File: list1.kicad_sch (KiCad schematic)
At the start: 3 parts, among them U1 8284A, U2 8259A, U3 8088

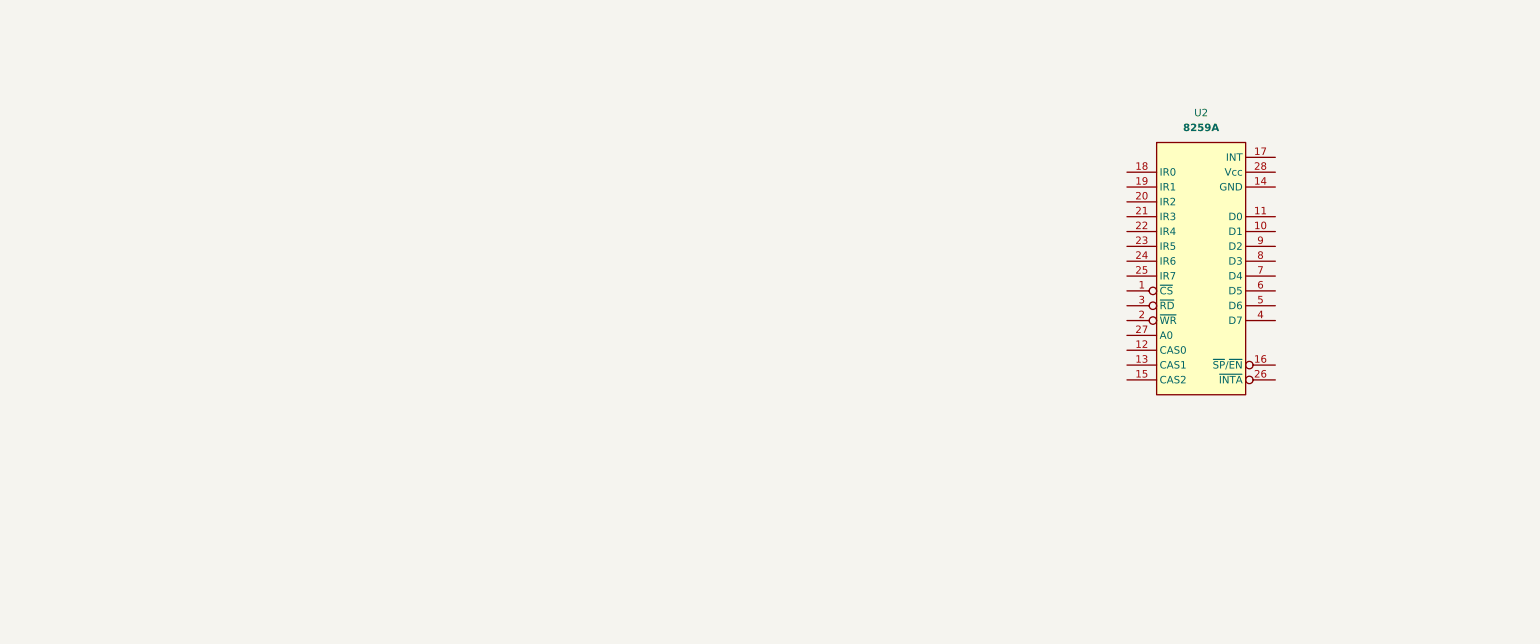
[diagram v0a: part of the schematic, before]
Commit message: Update 16.04.2024
Two datasheets added (8087 and 8288), library updated.
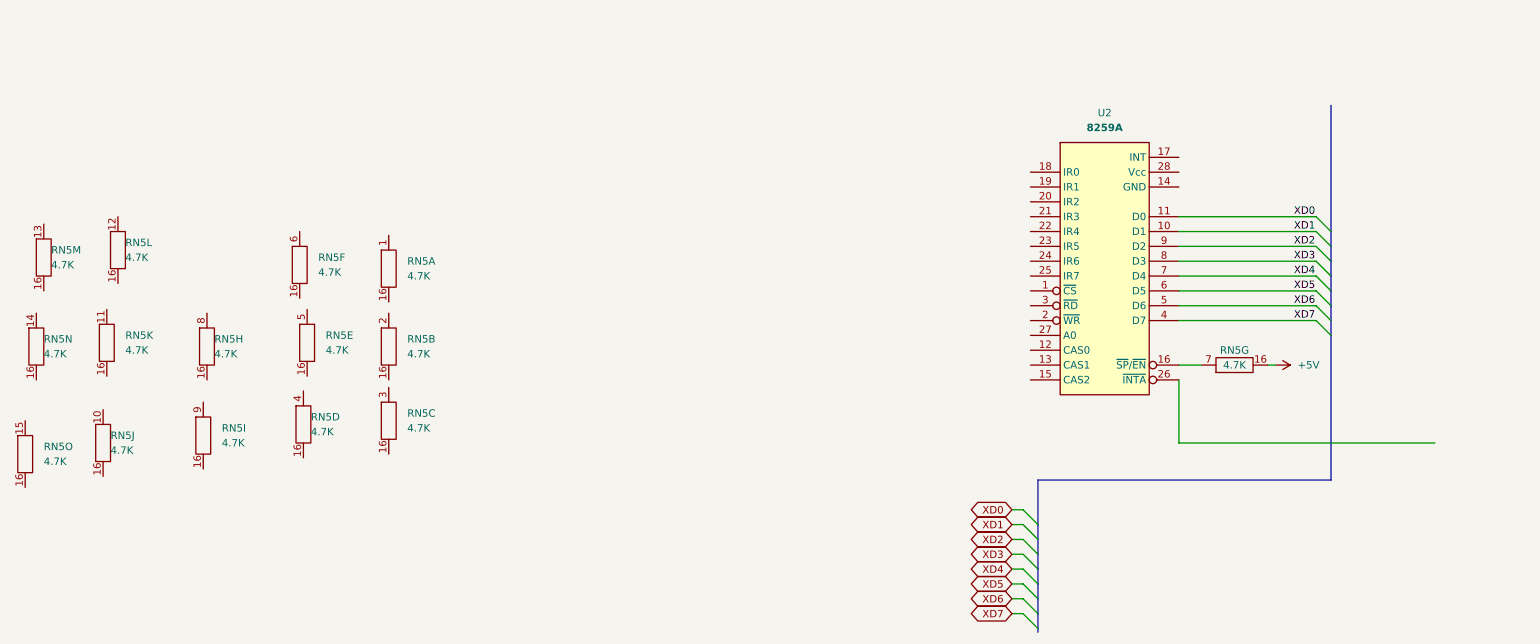
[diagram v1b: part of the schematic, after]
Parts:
- added RN5: 4.7K, Package_DIP:DIP-16_W7.62mm, symbol Mad5150_early:Resistor_Network
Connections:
- net XD1: now reaches U2.10 (D1)
- net XD0: now reaches U2.11 (D0)
- net at U2.16 (~{SP}/~{EN}): now also RN5.7
- net XD7: now reaches U2.4 (D7)
- net XD6: now reaches U2.5 (D6)
- net XD5: now reaches U2.6 (D5)
- net XD4: now reaches U2.7 (D4)
- net XD3: now reaches U2.8 (D3)
- net XD2: now reaches U2.9 (D2)
- new net +5V: RN5.16
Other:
- moved on the sheet: U2

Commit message: Update 17.04.2024
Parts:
- added C1: 5-30pf, symbol Device:C_Variable
- added R1, R2: 510, symbol Device:R
- added RN1: 4.7K, Package_DIP:DIP-16_W7.62mm, symbol Mad5150_early:Resistor_Network
- added U22: 74LS04, Package_DIP:DIP-14_W7.62mm, symbol 74xx:74LS04
- added Y1: 14.31818MHz, symbol Device:Crystal
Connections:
- net +5V: now also U1.18 (Vcc), U1.7 (~{AEN2}), U2.28 (Vcc), RN1.16
- net GND: now reaches U1.1 (CSYNC)
- net GND: now also U1.15 (~{ASYNC}), U1.6 (RDY2), U1.9 (GND), U2.14 (GND), R1.2, R2.2
- net at U1.13 (F/~{C}): now also U22.10
- net at U1.16 (X2): now also R2.1, Y1.1
- net at U1.17 (X1): now also C1.2, R1.1
- net ~{RDY}'/WAIT: now reaches U1.3 (~{AEN1})
- net ~{DMAWAIT}': now reaches U1.4 (RDY1)
- net ~{INTRCS}': now reaches U2.1 (~{CS})
- net IRQ0: now reaches U2.18 (IR0)
- net IRQ1: now reaches U2.19 (IR1)
- net ~{XIOW}': now reaches U2.2 (~{WR})
- net IRQ2: now reaches U2.20 (IR2)
- net IRQ3: now reaches U2.21 (IR3)
- net IRQ4: now reaches U2.22 (IR4)
- net IRQ5: now reaches U2.23 (IR5)
- net IRQ6: now reaches U2.24 (IR6)
- net IRQ7: now reaches U2.25 (IR7)
- net XA0: now reaches U2.27 (A0)
- net ~{XIOR}': now reaches U2.3 (~{RD})
- new net: RN1.11, U22.11
- new net: C1.1, Y1.2
- no-connect marks 0 -> 4
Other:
- moved on the sheet: RN5G, U1, U2

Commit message: Small update 18.04.2024
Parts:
- added C2: 0.047uF, symbol Device:C
- added U4: 8087, Package_DIP:DIP-40_W15.24mm_Socket_LongPads, symbol Mad5150_early:8087
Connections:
- net +5V: now also RN1.16, U3.40 (VCC), C2.1
- net GND: now also U3.1 (GND), U3.20 (GND), U3.33 (MN/~{MX}), C2.2
- net AD6: now reaches U3.10 (AD6)
- net AD5: now reaches U3.11 (AD5)
- net AD4: now reaches U3.12 (AD4)
- net AD3: now reaches U3.13 (AD3)
- net AD2: now reaches U3.14 (AD2)
- net AD1: now reaches U3.15 (AD1)
- net AD0: now reaches U3.16 (AD0)
- net NMI: now reaches U3.17 (NMI)
- net CLK88: now reaches U3.19 (CLK)
- net CLK88: now also U1.8 (CLK)
- net RESET: now reaches U3.21 (RESET)
- net RESET: now also U1.10 (RESET)
- net READY: now reaches U3.22 (READY)
- net READY: now also U1.5 (READY)
- net QS1: now reaches U3.24 (QS1)
- net QS0: now reaches U3.25 (QS0)
- net ~{RQ/GT1}: now reaches U3.30 (~{RQ/GT1})
- net at U3.31 (~{RQ/GT0}): now also RN1.15
- net AD7: now reaches U3.9 (AD7)
- no-connect marks 4 -> 6
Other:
- moved on the sheet: C1, R1, R2, RN1K, RN5G, U1, U2, U22E, U3, Y1

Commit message: First PCB draw
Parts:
- renumbered U2 to U25
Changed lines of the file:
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@@
   (symbol (lib_id "Mad5150_early:8259A") (at 99.695 123.825 0) (unit 1)
     (in_bom yes) (on_board yes) (dnp no)
-    (property "Reference" "U2" (at 99.695 114.3 0)
+    (property "Reference" "U25" (at 99.695 114.3 0)
       (effects (font (size 1.27 1.27)))
     )
@@
       (project "Mad5160"
         (path "/ac3c86ab-084e-42f6-87ca-c4b0142d8ff2/921209e9-21b1-4dfe-a217-0f57a16b1ecc"
-          (reference "U2") (unit 1)
+          (reference "U25") (unit 1)
         )
       )

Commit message: Update 19/04
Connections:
- net +5V: now also RN1.16
- net ~{RQ/GT1}: now also RN1.12
- net at U3.18 (INTR): now also U25.17 (INT)
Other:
- moved on the sheet: RN1L
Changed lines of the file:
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@@
   (junction (at 116.205 50.165) (diameter 0) (color 0 0 0 0)
+  )
+  (junction (at 179.07 74.295) (diameter 0) (color 0 0 0 0)
   )
   (junction (at 215.265 36.195) (diameter 0) (color 0 0 0 0)
@@
     (stroke (width 0) (type default))
   )
-  (bus_entry (at 166.37 53.975) (size 2.54 -2.54)
-    (stroke (width 0) (type default))
-  )
   (bus_entry (at 166.37 74.295) (size 2.54 -2.54)
     (stroke (width 0) (type default))
@@
     (stroke (width 0) (type default))
   )
+  (wire (pts (xy 179.07 80.645) (xy 179.07 74.295))
+    (stroke (width 0) (type default))
+  )
   (bus (pts (xy 138.43 125.095) (xy 138.43 127.635))
     (stroke (width 1) (type default))
@@
     (stroke (width 0) (type default))
   )
-  (bus (pts (xy 166.37 51.435) (xy 166.37 53.975))
-    (stroke (width 1) (type default))
-  )
   (wire (pts (xy 112.395 62.865) (xy 129.54 62.865))
     (stroke (width 0) (type default))
@@
     (stroke (width 0) (type default))
   )
+  (wire (pts (xy 179.07 74.295) (xy 186.055 74.295))
+    (stroke (width 0) (type default))
+  )
   (wire (pts (xy 75.565 73.025) (xy 86.995 73.025))
     (stroke (width 0) (type default))
@@
     (stroke (width 0) (type default))
   )
+  (wire (pts (xy 112.395 104.775) (xy 161.925 104.775))
+    (stroke (width 0) (type default))
+  )
   (wire (pts (xy 74.93 135.255) (xy 86.995 135.255))
     (stroke (width 0) (type default))
@@
     (stroke (width 0) (type default))
   )
+  (wire (pts (xy 178.435 92.075) (xy 179.07 92.075))
+    (stroke (width 0) (type default))
+  )
   (bus (pts (xy 166.37 71.755) (xy 166.37 74.295))
     (stroke (width 1) (type default))
@@
     (stroke (width 0) (type default))
   )
+  (wire (pts (xy 159.385 52.705) (xy 159.385 94.615))
+    (stroke (width 0) (type default))
+  )
   (bus (pts (xy 88.265 160.02) (xy 138.43 160.02))
     (stroke (width 1) (type default))
@@
     (stroke (width 0) (type default))
   )
+  (wire (pts (xy 161.925 104.775) (xy 161.925 41.275))
+    (stroke (width 0) (type default))
+  )
   (wire (pts (xy 201.295 17.145) (xy 215.265 17.145))
     (stroke (width 0) (type default))
   )
-  (wire (pts (xy 168.91 74.295) (xy 186.055 74.295))
+  (wire (pts (xy 168.91 74.295) (xy 179.07 74.295))
     (stroke (width 0) (type default))
   )
@@
     (stroke (width 1) (type default))
   )
-  (bus (pts (xy 166.37 53.975) (xy 166.37 56.515))
+  (bus (pts (xy 166.37 51.435) (xy 166.37 56.515))
     (stroke (width 1) (type default))
   )
@@
     (stroke (width 0) (type default))
   )
+  (wire (pts (xy 168.275 51.435) (xy 168.275 52.705))
+    (stroke (width 0) (type default))
+  )
   (wire (pts (xy 85.09 83.185) (xy 85.725 83.185))
     (stroke (width 0) (type default))
@@
     (stroke (width 0) (type default))
   )
+  (wire (pts (xy 186.055 51.435) (xy 168.275 51.435))
+    (stroke (width 0) (type default))
+  )
   (bus (pts (xy 138.43 117.475) (xy 138.43 120.015))
     (stroke (width 1) (type default))
@@
     (stroke (width 0) (type default))
   )
-  (wire (pts (xy 168.91 51.435) (xy 186.055 51.435))
-    (stroke (width 0) (type default))
-  )
   (wire (pts (xy 168.91 69.215) (xy 186.055 69.215))
     (stroke (width 0) (type default))
   )
+  (wire (pts (xy 159.385 52.705) (xy 168.275 52.705))
+    (stroke (width 0) (type default))
+  )
   (wire (pts (xy 83.82 167.64) (xy 85.725 167.64))
     (stroke (width 0) (type default))
@@
     (stroke (width 0) (type default))
   )
+  (wire (pts (xy 178.435 92.075) (xy 178.435 93.345))
+    (stroke (width 0) (type default))
+  )
   (wire (pts (xy 168.91 79.375) (xy 186.055 79.375))
     (stroke (width 0) (type default))
@@
     (stroke (width 0) (type default))
   )
+  (wire (pts (xy 161.925 41.275) (xy 186.055 41.275))
+    (stroke (width 0) (type default))
+  )
   (bus (pts (xy 88.265 172.72) (xy 88.265 170.18))
     (stroke (width 1) (type default))
@@
     (stroke (width 0) (type default))
   )
+  (wire (pts (xy 159.385 94.615) (xy 74.295 94.615))
+    (stroke (width 0) (type default))
+  )
   (wire (pts (xy 112.395 142.875) (xy 112.395 153.67))
     (stroke (width 0) (type default))
@@
   (bus (pts (xy 88.265 170.18) (xy 88.265 167.64))
     (stroke (width 1) (type default))
+  )
+  (wire (pts (xy 178.435 93.345) (xy 174.625 93.345))
+    (stroke (width 0) (type default))
   )
   (label "AD7" (at 169.545 71.755 0) (fields_autoplaced)
@@
     (effects (font (size 1.27 1.27)) (justify left bottom))
   )
-  (label "NMI" (at 169.545 51.435 0) (fields_autoplaced)
+  (label "NMI" (at 178.435 51.435 0) (fields_autoplaced)
     (effects (font (size 1.27 1.27)) (justify left bottom))
   )
@@
     (effects (font (size 1.27 1.27)) (justify right))
     (property "Intersheetrefs" "${INTERSHEET_REFS}" (at 76.0345 165.1 0)
+      (effects (font (size 1.27 1.27)) (justify right) hide)
+    )
+  )
+  (global_label "NMI" (shape input) (at 74.295 94.615 180) (fields_autoplaced)
+    (effects (font (size 1.27 1.27)) (justify right))
+    (property "Intersheetrefs" "${INTERSHEET_REFS}" (at 67.9231 94.615 0)
       (effects (font (size 1.27 1.27)) (justify right) hide)
     )
@@
     )
   )
-  (symbol (lib_id "Mad5150_early:Resistor_Network") (at 284.48 -78.74 0) (unit 12)
-    (in_bom yes) (on_board yes) (dnp no) (fields_autoplaced)
-    (property "Reference" "RN1" (at 288.29 -79.375 0)
-      (effects (font (size 1.27 1.27)) (justify left))
-    )
-    (property "Value" "4.7K" (at 288.29 -76.835 0)
-      (effects (font (size 1.27 1.27)) (justify left))
-    )
-    (property "Footprint" "Package_DIP:DIP-16_W7.62mm" (at 284.48 -78.74 0)
-      (effects (font (size 1.27 1.27)) hide)
-    )
-    (property "Datasheet" "" (at 285.115 -79.375 0)
-      (effects (font (size 1.27 1.27)) hide)
-    )
+  (symbol (lib_id "power:+5V") (at 174.625 93.345 90) (unit 1)
+    (in_bom yes) (on_board yes) (dnp no) (fields_autoplaced)
+    (property "Reference" "#PWR014" (at 178.435 93.345 0)
+      (effects (font (size 1.27 1.27)) hide)
+    )
+    (property "Value" "+5V" (at 171.45 93.98 90)
+      (effects (font (size 1.27 1.27)) (justify left))
+    )
+    (property "Footprint" "" (at 174.625 93.345 0)
+      (effects (font (size 1.27 1.27)) hide)
+    )
+    (property "Datasheet" "" (at 174.625 93.345 0)
+      (effects (font (size 1.27 1.27)) hide)
+    )
+    (pin "1")
+    (instances
+      (project "Mad5160"
+        (path "/ac3c86ab-084e-42f6-87ca-c4b0142d8ff2/921209e9-21b1-4dfe-a217-0f57a16b1ecc"
+          (reference "#PWR014") (unit 1)
+        )
+      )
+    )
+  )
+  (symbol (lib_id "Mad5150_early:Resistor_Network") (at 179.07 86.36 0) (unit 12)
+    (in_bom yes) (on_board yes) (dnp no)
+    (property "Reference" "RN1" (at 172.72 85.09 0)
+      (effects (font (size 1.27 1.27)) (justify left))
+    )
+    (property "Value" "4.7K" (at 173.355 86.995 0)
+      (effects (font (size 1.27 1.27)) (justify left))
+    )
+    (property "Footprint" "Package_DIP:DIP-16_W7.62mm" (at 179.07 86.36 0)
+      (effects (font (size 1.27 1.27)) hide)
+    )
+    (property "Datasheet" "" (at 179.705 85.725 0)
+      (effects (font (size 1.27 1.27)) hide)
+    )

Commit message: First list finished
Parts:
- added C8: 0.047uF, symbol Device:C
- added U2: LS245, Package_DIP:DIP-20_W7.62mm, symbol Mad5150_early:LS245_U2
- added U5: LS373, Package_DIP:DIP-20_W7.62mm, symbol Mad5150_early:LS373_U5
- added U6: LS244, Package_DIP:DIP-20_W7.62mm, symbol Mad5150_early:LS244_U6
- added U7: LS373, Package_DIP:DIP-20_W7.62mm, symbol Mad5150_early:LS373_U7
- added U8: 8288, Package_DIP:DIP-20_W7.62mm, symbol Mad5150_early:8288
- Y1: footprint (none) -> Crystal:Crystal_HC49-U_Horizontal
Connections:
- net ~{RQ/GT1} is gone; now on net ~{RQ/GT}': RN1.12, U3.30 (~{RQ/GT1})
- net +5V: now also RN1.16, RN1.16, RN5.16, RN5.16, RN5.16, RN5.16, RN5.16, U4.33 (RQ/GT1), U4.34 (BHE/S7), U4.40 (Vcc), C8.1, U8.20 (Vcc)
- net AD0: now also U4.16 (AD0), U2.9 (A7), U5.8 (D3)
- net AD1: now also U4.15 (AD1), U2.8 (A6), U5.13 (D4)
- net AD2: now also U4.14 (AD2), U2.7 (A5), U5.14 (D5)
- net AD3: now also U4.13 (AD3), U2.6 (A4), U5.7 (D2)
- net AD4: now also U4.12 (AD4), U2.5 (A3), U5.4 (D1)
- net AD5: now also U4.11 (AD5), U2.4 (A2), U5.17 (D6)
- net AD6: now also U4.10 (AD6), U2.3 (A1), U5.18 (D7)
- net AD7: now also U4.9 (AD7), U2.2 (A0), U5.3 (D0)
- net CLK88: now also U4.19 (CLK), U8.2 (CLK)
- net GND: now also U4.1 (GND), U4.20 (GND), C8.2, U8.1 (IOB), U8.10 (GND)
- net QS0: now also U4.25 (QS0)
- net QS1: now also U4.24 (QS1)
- net READY: now also U4.22 (READY)
- net RESET: now also U4.21 (RESET)
- net AA14: now reaches U3.2 (A14)
- net AA14: now also U4.2 (AD14), U7.14 (D5)
- net at U3.23 (~{TEST}): now also RN1.13, U4.23 (BUSY)
- net ~{S0}': now reaches U3.26 (~{S0})
- net ~{S0}': now also U4.26 (~{S0}), U8.19 (~{S0})
- net ~{S1}': now reaches U3.27 (~{S1})
- net ~{S1}': now also U4.27 (~{S1}), U8.3 (~{S1})
- net ~{S2}': now reaches U3.28 (~{S2})
- net ~{S2}': now also U4.28 (~{S2}), U8.18 (~{S2})
- net ~{LOCK}': now reaches U3.29 (LOCK)
- net AA13: now reaches U3.3 (A13)
- net AA13: now also U4.3 (AD13), U7.8 (D3)
- net AA19: now reaches U3.35 (A19)
- net AA19: now also U4.35 (A19), U7.18 (D7)
- net AA18: now reaches U3.36 (A18)
- net AA18: now also U4.36 (A18), U7.3 (D0)
- net AA17: now reaches U3.37 (A17)
- net AA17: now also U4.37 (A17), U7.4 (D1)
- net AA16: now reaches U3.38 (A16)
- net AA16: now also U4.38 (A16), U7.17 (D6)
- net AA15: now reaches U3.39 (A15)
- net AA15: now also U4.39 (AD15), U7.7 (D2)
- net AA12: now reaches U3.4 (A12)
- net AA12: now also U4.4 (AD12), U7.13 (D4)
- net AA11: now reaches U3.5 (A11)
- net AA11: now also U4.5 (AD11), U6.8 (I3a)
- net AA10: now reaches U3.6 (A10)
- net AA10: now also U4.6 (AD10), U6.6 (I2a)
- net AA9: now reaches U3.7 (A9)
- net AA9: now also U4.7 (AD9), U6.4 (I1a)
- net AA8: now reaches U3.8 (A8)
- net AA8: now also U4.8 (AD8), U6.2 (I0a)
- net OSC: now reaches U1.12 (OSC)
- net PCLK: now reaches U1.2 (PCLK)
- net ~{INTA}': now reaches RN1.9
- net ~{INTA}': now also U25.26 (~{INTA}), U8.14 (~{INTA})
- net ~{MEMW}': now reaches RN5.15
- net ~{MEMW}': now also U8.8 (~{AMWC})
- net ~{IOR}': now reaches RN5.12
- net ~{IOR}': now also U8.13 (~{IORC})
- net ~{MEMR}': now reaches RN5.6
- net ~{MEMR}': now also U8.7 (~{MRDC})
- net ~{MWTC}': now reaches RN5.14
- net ~{MWTC}': now also U8.9 (~{MWTC})
- net ~{RQ/GT}': now reaches U4.31 (~{RQ/GT0})
- net N.P. NPI: now reaches U4.32 (INT)
- net ~{IOW}': now reaches RN5.13
- net ~{IOW}': now also U8.12 (~{AIOWC})
- net at U22.12: now also U2.19 (CE)
- net at U22.13: now also U8.16 (DEN)
- new net: U2.1 (A->B), U8.4 (DT/~{R})
- new net A0: U5.9 (O3)
- new net A1: U5.12 (O4)
- new net A10: U6.14 (O2a)
- new net A11: U6.12 (O3a)
- new net A12: U7.12 (O4)
- new net A13: U7.9 (O3)
- new net A14: U7.15 (O5)
- new net A15: U7.6 (O2)
- new net A16: U7.16 (O6)
- new net A17: U7.5 (O1)
- new net A18: U7.2 (O0)
- new net A19: U7.19 (O7)
- new net A2: U5.15 (O5)
- new net A3: U5.6 (O2)
- new net A4: U5.5 (O1)
- new net A5: U5.16 (O6)
- new net A6: U5.19 (O7)
- new net A7: U5.2 (O0)
- new net A8: U6.18 (O0a)
- new net A9: U6.16 (O1a)
- new net AENBRD: U8.6 (~{AEN})
- new net ALE: U5.11 (LE), U7.11 (LE), U8.5 (ALE)
- new net D0: U2.11 (B7)
- new net D1: U2.12 (B6)
- new net D2: U2.13 (B5)
- new net D3: U2.14 (B4)
- new net D4: U2.15 (B3)
- new net D5: U2.16 (B2)
- new net D6: U2.17 (B1)
- new net D7: U2.18 (B0)
- new net ~{AEN}': U5.1 (~{OE}), U6.1 (OEa), U7.1 (~{OE}), U8.15 (CEN)
- no-connect marks 6 -> 17
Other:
- moved on the sheet: C1, C2, R1, R2, RN1F, RN1I, RN1K, RN1L, RN1M, RN1O, RN5F, RN5G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
